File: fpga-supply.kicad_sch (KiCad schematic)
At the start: 64 parts, among them U1 MPFS250T-FCVG484

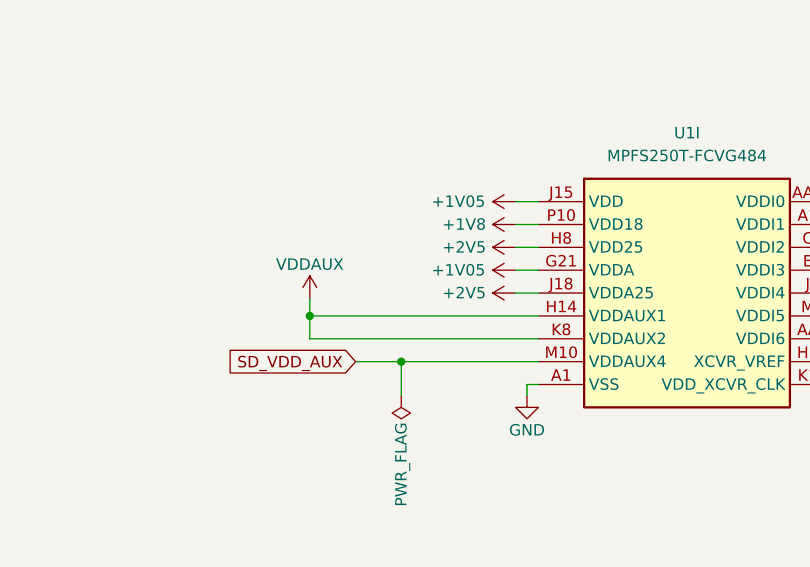
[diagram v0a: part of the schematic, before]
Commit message: [#59910] Align buses, updated symbols and clean ERC
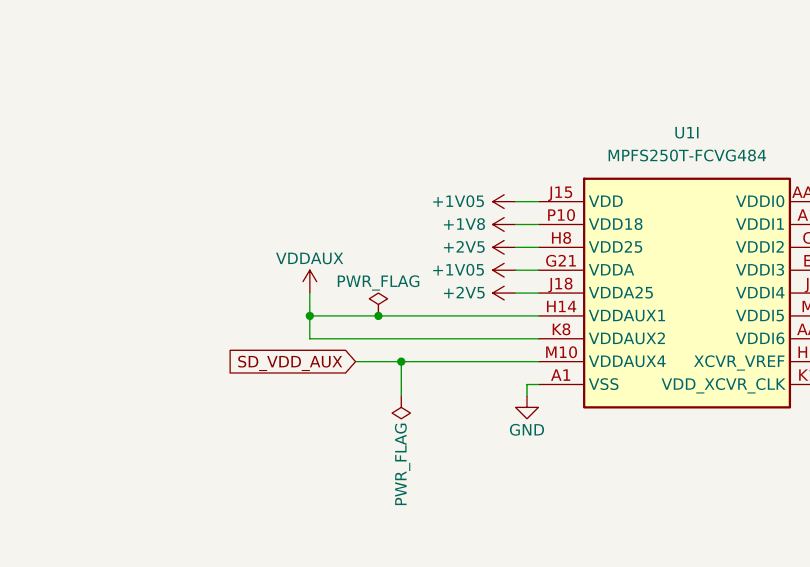
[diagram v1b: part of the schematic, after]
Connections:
- net VDDI renamed VDD

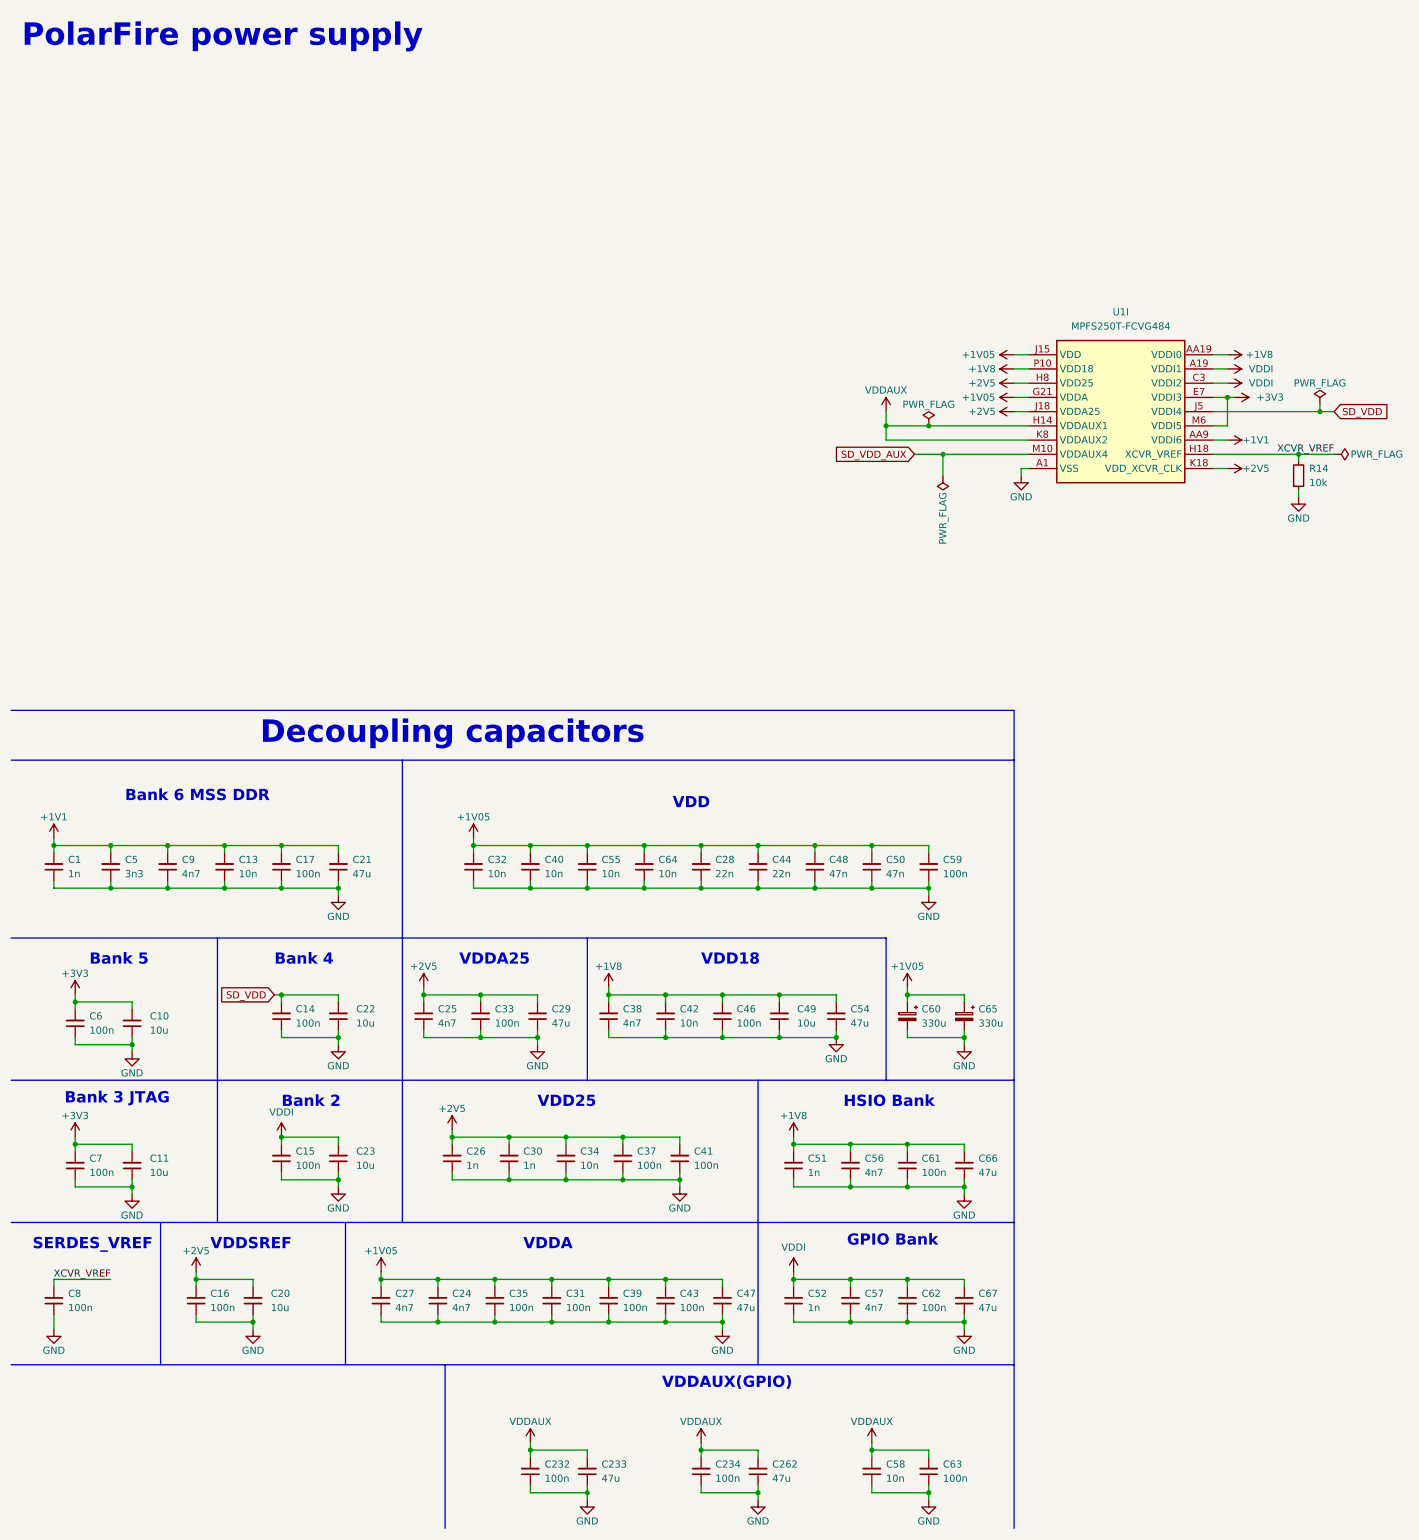
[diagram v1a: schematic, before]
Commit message: [#73079] Migrate project to KiCad 8. Clean DRCs
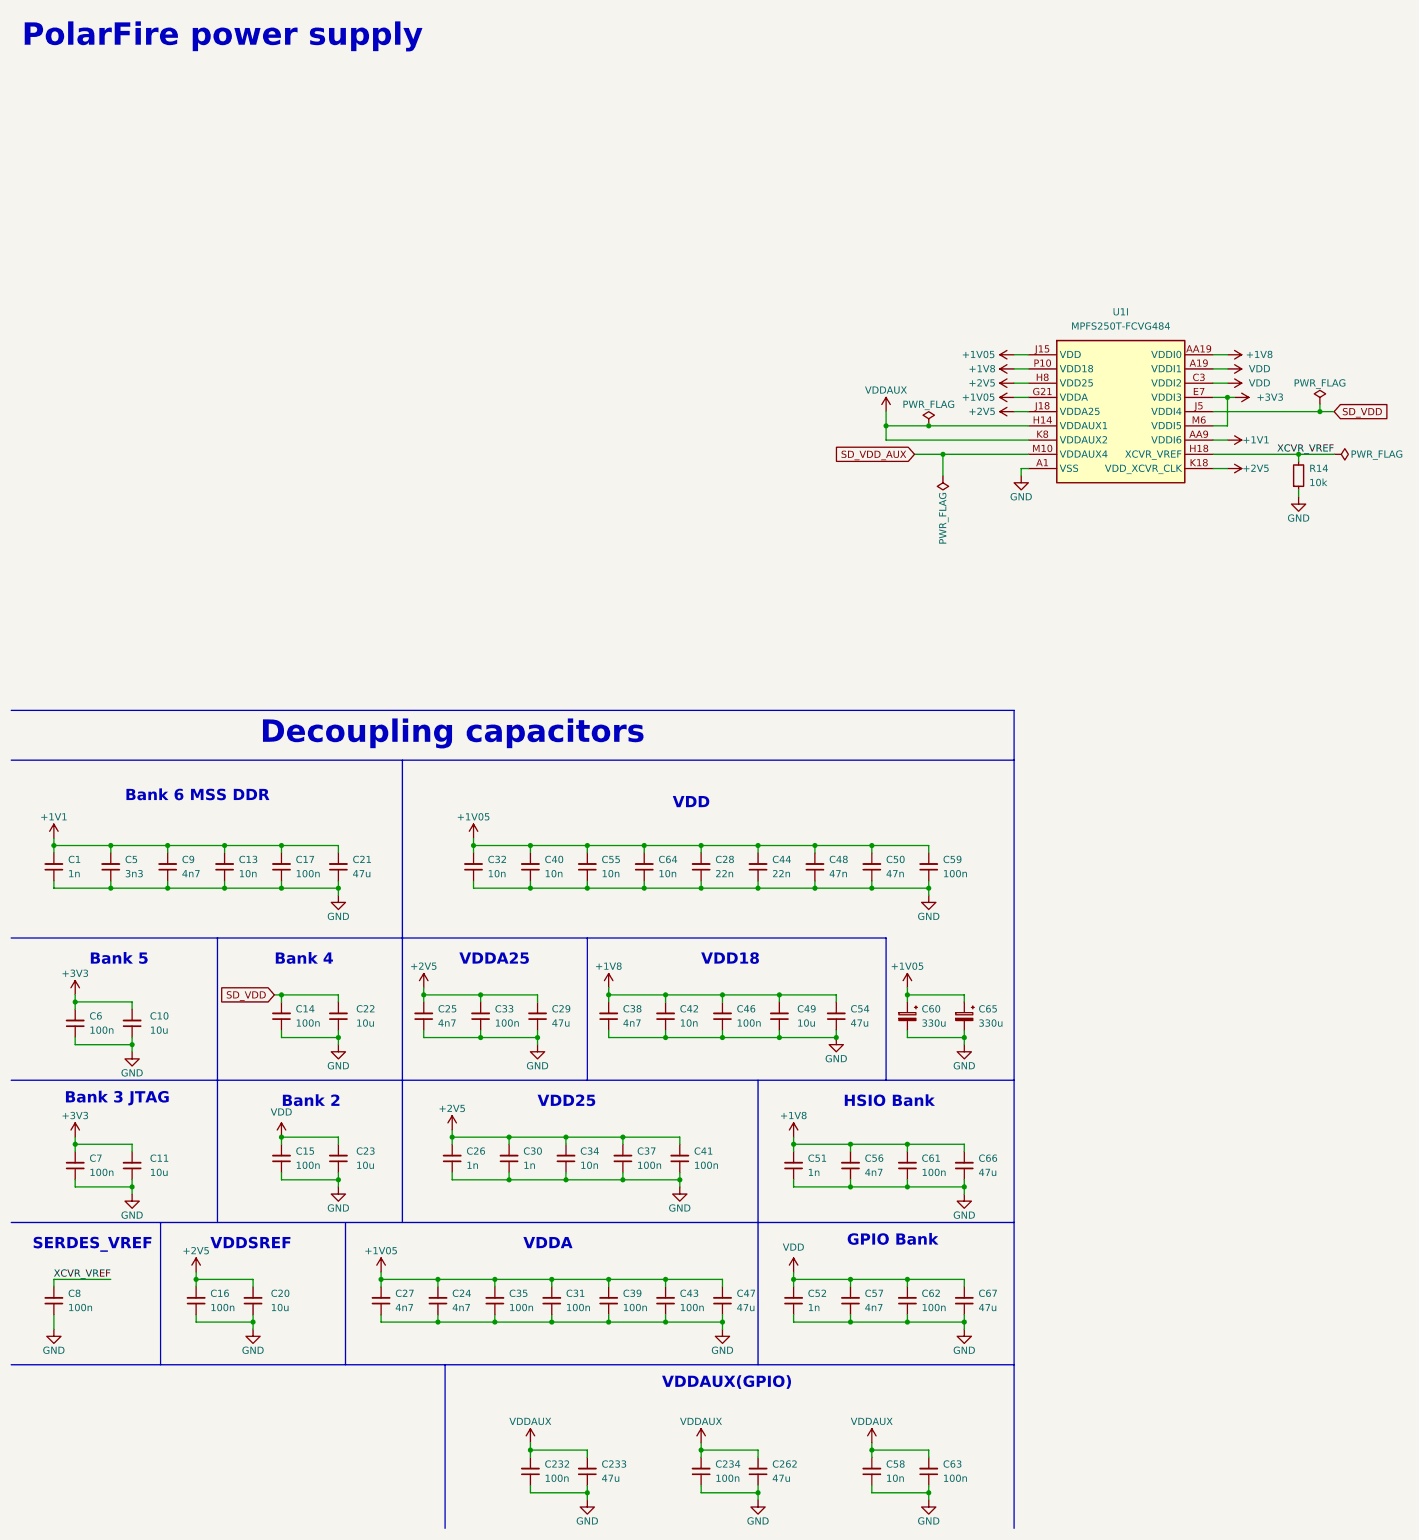
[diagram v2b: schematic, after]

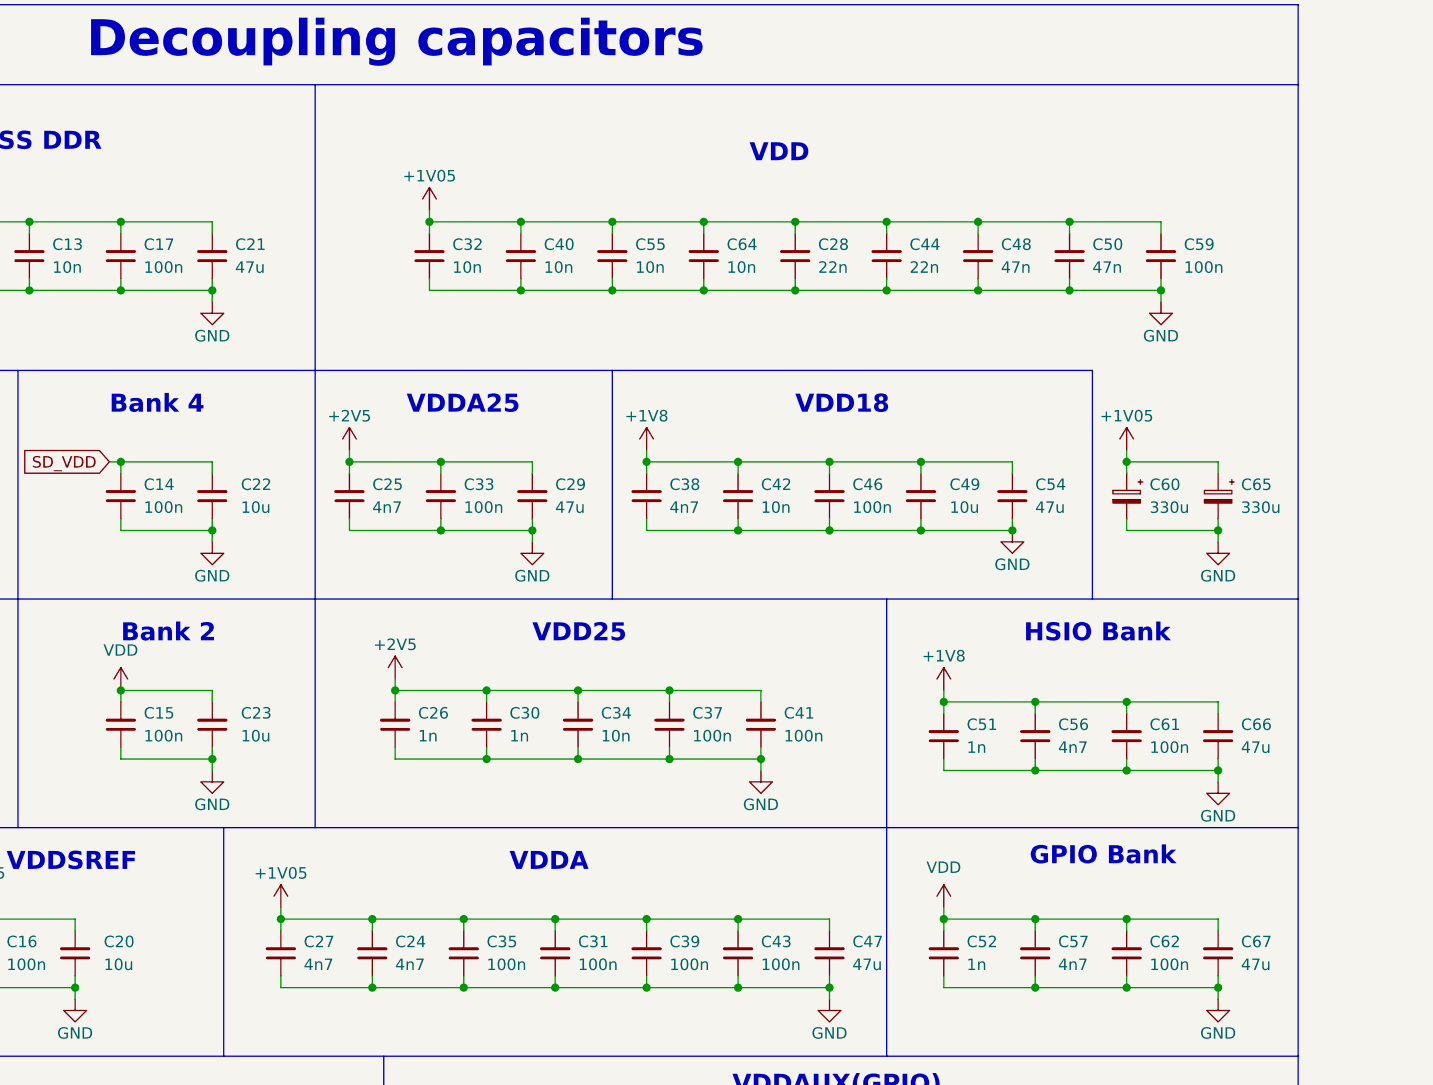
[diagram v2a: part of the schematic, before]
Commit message: [#73079] Update symbols, clean ERC
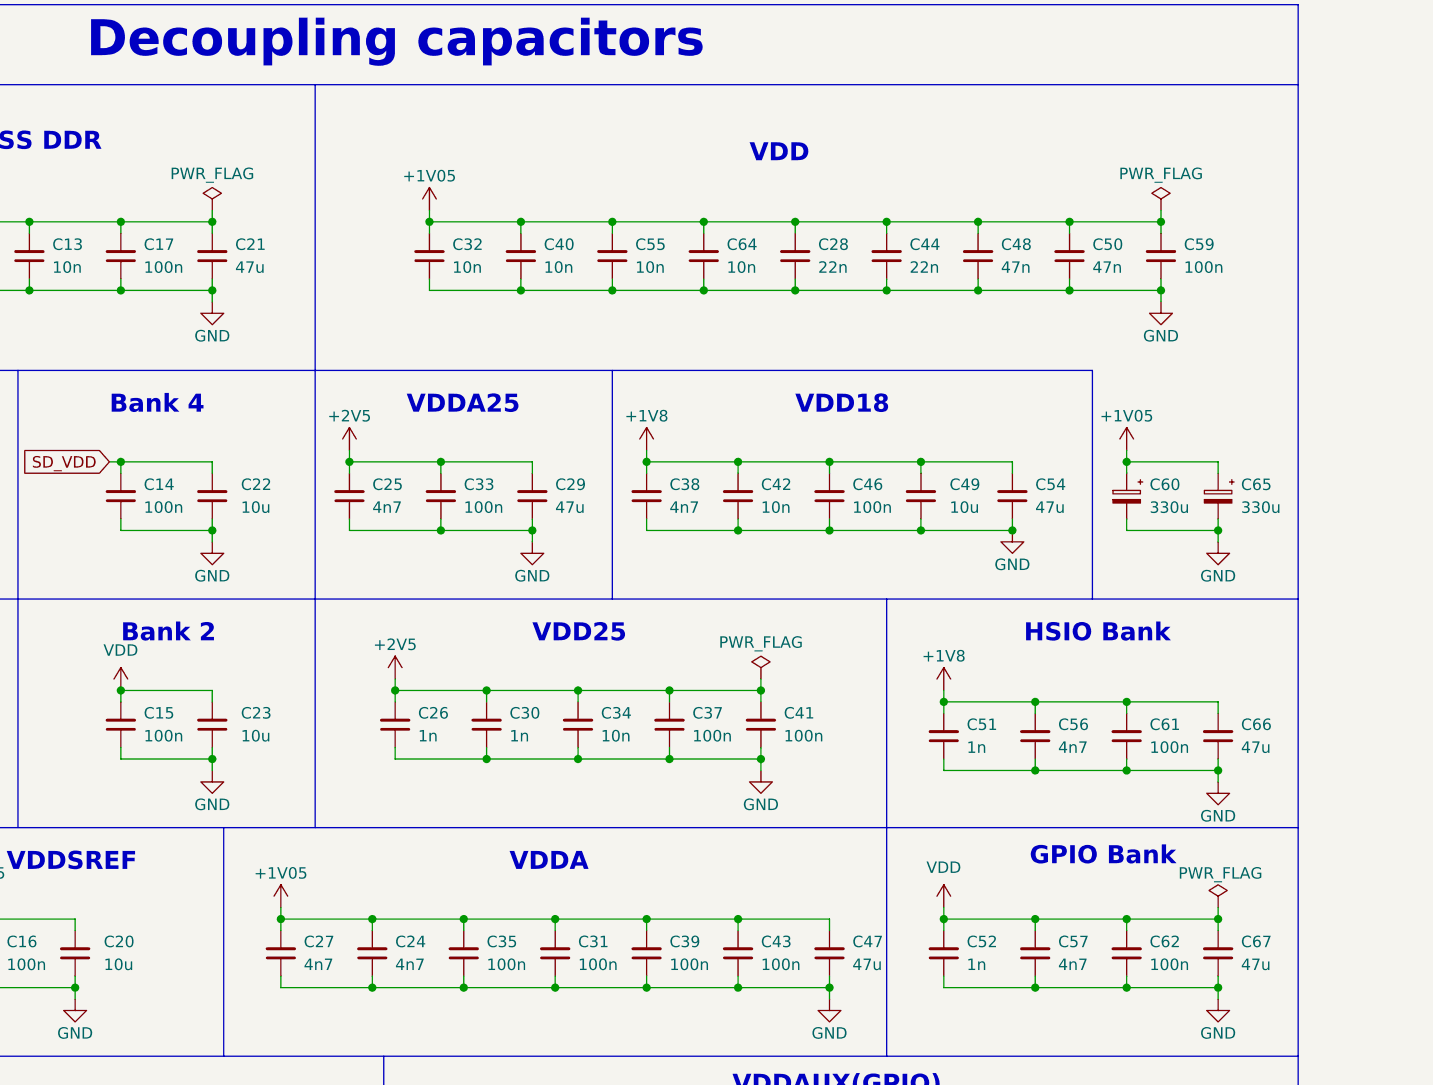
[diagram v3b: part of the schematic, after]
